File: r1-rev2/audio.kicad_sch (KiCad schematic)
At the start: 24 parts, among them J3 HP_3.5mm, J4 LO_3.5mm, Q4 AO3401A, U15 TPAZ1143-04F, U16 TPAZ1143-04F, U3 TLV320AIC3104

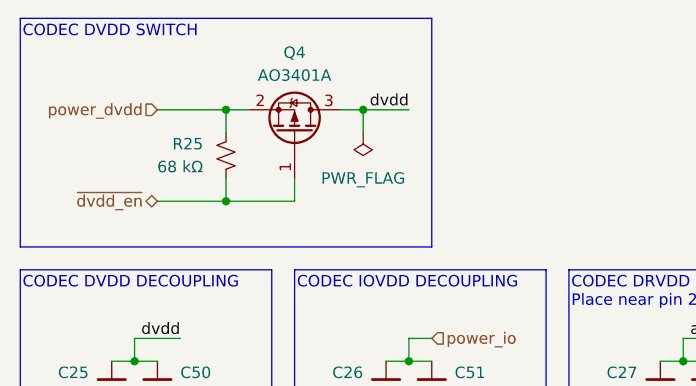
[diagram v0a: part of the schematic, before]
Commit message: Fix symbol library links & resync footprints from KiCAD libraries
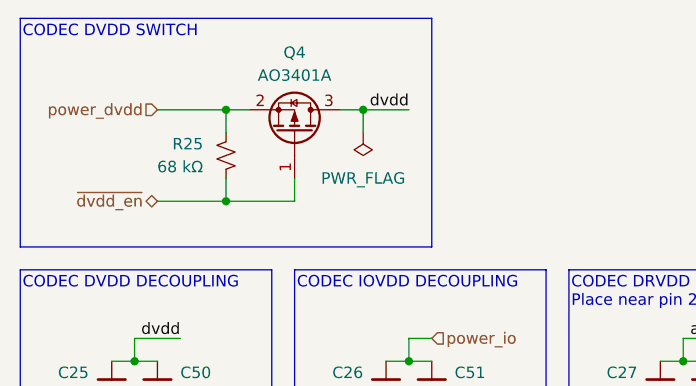
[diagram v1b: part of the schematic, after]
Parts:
- Q4: symbol Device:Q_PMOS_GSD -> Transistor_FET:Q_PMOS_GSD
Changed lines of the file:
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@@
 	)
 	(symbol
-		(lib_id "Device:Q_PMOS_GSD")
+		(lib_id "Transistor_FET:Q_PMOS_GSD")
 		(at 83.82 27.94 270)
 		(mirror x)
